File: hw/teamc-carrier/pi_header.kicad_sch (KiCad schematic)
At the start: 6 parts, among them J1 RPi 3 A+ GPIO, J13 UART console

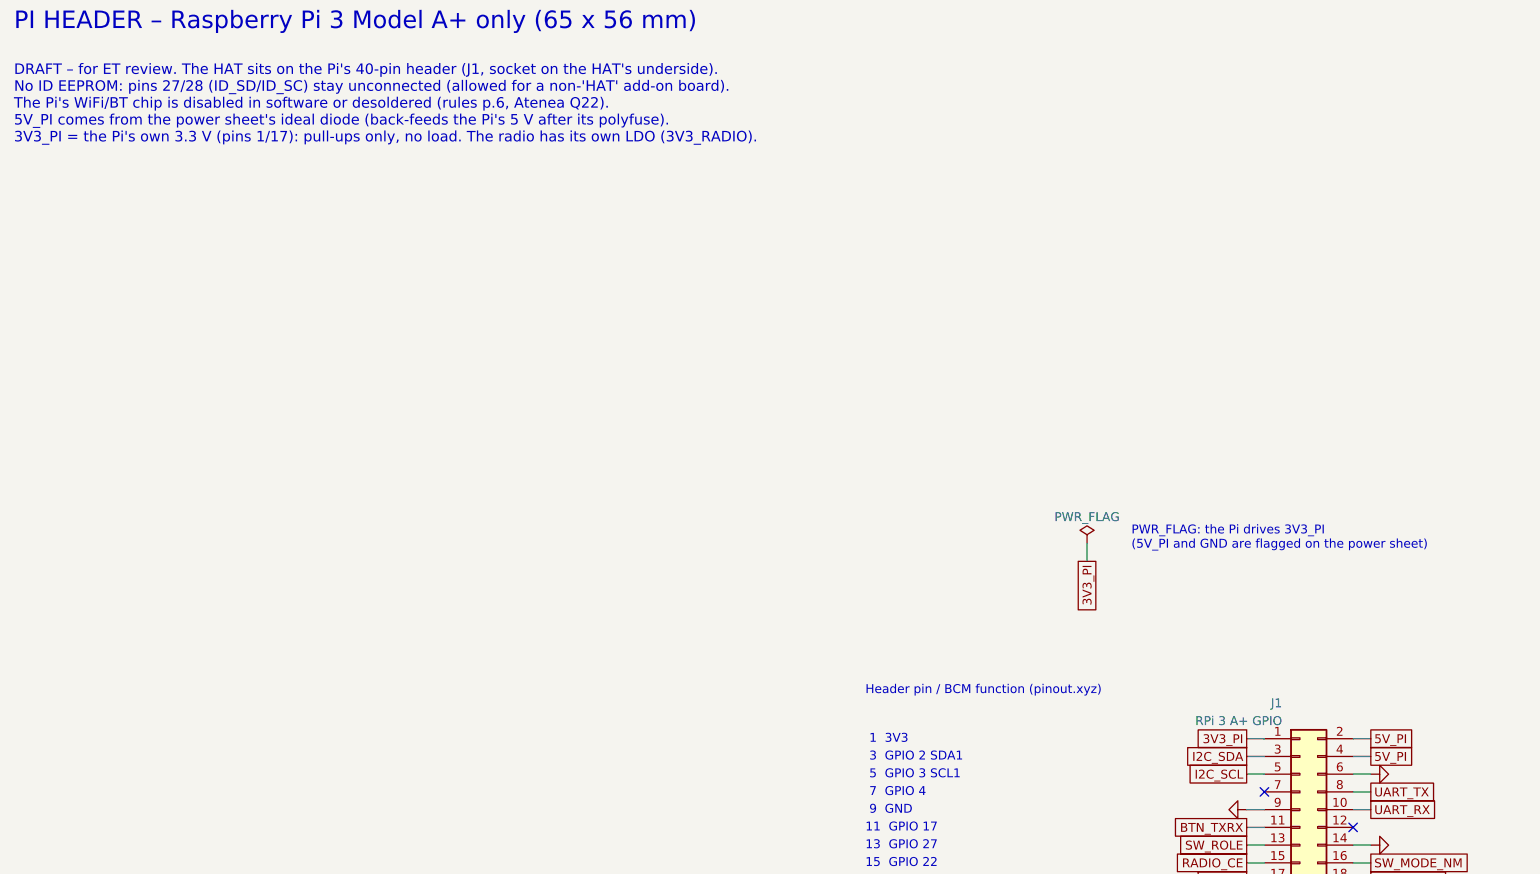
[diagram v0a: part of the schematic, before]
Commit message: carrier: review fixes (Si2333DDS, BCM857BS, fuse, soft start, D_SMF, pull-ups to 3V3_PI, MODE->VIN), power+SPI routed (DRC 0 errors), GND vias, BoM, design notes; CLAUDE.md session log
Co-Authored-By: Claude Opus 5.5 <noreply@anthropic.com>
Claude-Session: https://claude.ai/code/session_01Dy4TuRNF8V28KreA3jwCtM
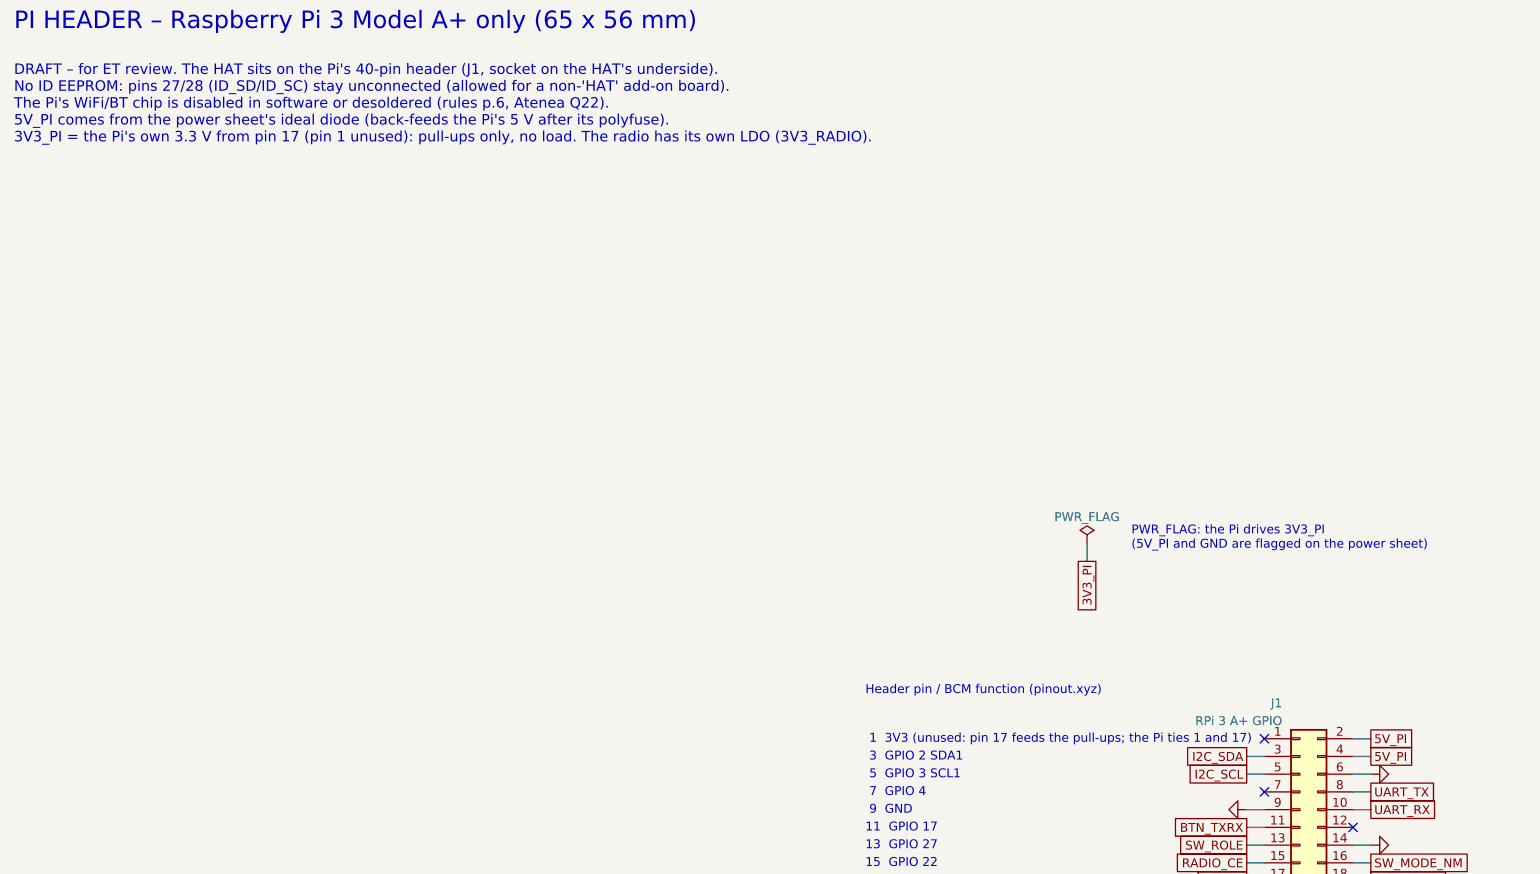
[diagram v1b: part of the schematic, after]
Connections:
- net 3V3_PI: no longer J1.1 (Pin_1)
- no-connect marks 10 -> 11
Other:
- note added: "1 3V3 (unused: pin 17 feeds the pull-ups; the Pi ties 1 and 17)"
- note removed: "1 3V3"
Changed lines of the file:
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@@
 		(comment 2 "Generated by hw/scripts/schgen.py; edit the sheet's .py, not this file")
 	)
-	(wire
-		(pts
-			(xy 204.47 124.46)
-			(xy 201.93 124.46)
-		)
-		(stroke
-			(width 0)
-			(type default)
-		)
-	)
-	(global_label "3V3_PI"
-		(shape passive)
-		(at 201.93 124.46 180)
-		(fields_autoplaced yes)
-		(effects
-			(font
-				(size 1.27 1.27)
-			)
-			(justify right)
-		)
+	(no_connect
+		(at 204.47 124.46)
 	)
 	(wire
@@
 		)
 	)
-	(text "DRAFT – for ET review. The HAT sits on the Pi's 40-pin header (J1, socket on the HAT's underside).\nNo ID EEPROM: pins 27/28 (ID_SD/ID_SC) stay unconnected (allowed for a non-'HAT' add-on board).\nThe Pi's WiFi/BT chip is disabled in software or desoldered (rules p.6, Atenea Q22).\n5V_PI comes from the power sheet's ideal diode (back-feeds the Pi's 5 V after its polyfuse).\n3V3_PI = the Pi's own 3.3 V (pins 1/17): pull-ups only, no load. The radio has its own LDO (3V3_RADIO)."
+	(text "DRAFT – for ET review. The HAT sits on the Pi's 40-pin header (J1, socket on the HAT's underside).\nNo ID EEPROM: pins 27/28 (ID_SD/ID_SC) stay unconnected (allowed for a non-'HAT' add-on board).\nThe Pi's WiFi/BT chip is disabled in software or desoldered (rules p.6, Atenea Q22).\n5V_PI comes from the power sheet's ideal diode (back-feeds the Pi's 5 V after its polyfuse).\n3V3_PI = the Pi's own 3.3 V from pin 17 (pin 1 unused): pull-ups only, no load. The radio has its own LDO (3V3_RADIO)."
 		(exclude_from_sim no)
 		(at 25.4 27.94 0)
@@
 		)
 	)
-	(text " 1  3V3"
+	(text " 1  3V3 (unused: pin 17 feeds the pull-ups; the Pi ties 1 and 17)"
 		(exclude_from_sim no)
 		(at 147.32 123.82 0)
